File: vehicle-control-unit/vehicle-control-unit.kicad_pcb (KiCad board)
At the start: 2 copper layers, 175.3 x 50.8 mm, 53 parts, among them J1 Conn_02x04_Male_UnitPerRow, J10 Connector:Screw_Terminal_01x02, J2 Conn_01x04_Male, J3 Conn_02x03_Male, J4 Conn_02x03_Male, J5 Conn_02x03_Male, J6 Conn_02x03_Male, J7 Conn_01x03_Male, J8 Conn_01x03_Male, J9 Conn_02x06_Male_UnitPerRow, Q1 BC517, SW1 SW_SPST, U1 Teensy3.2, U2 NRF24L01+ breakout, U3 ULN2803A, U4 MIC29502WT

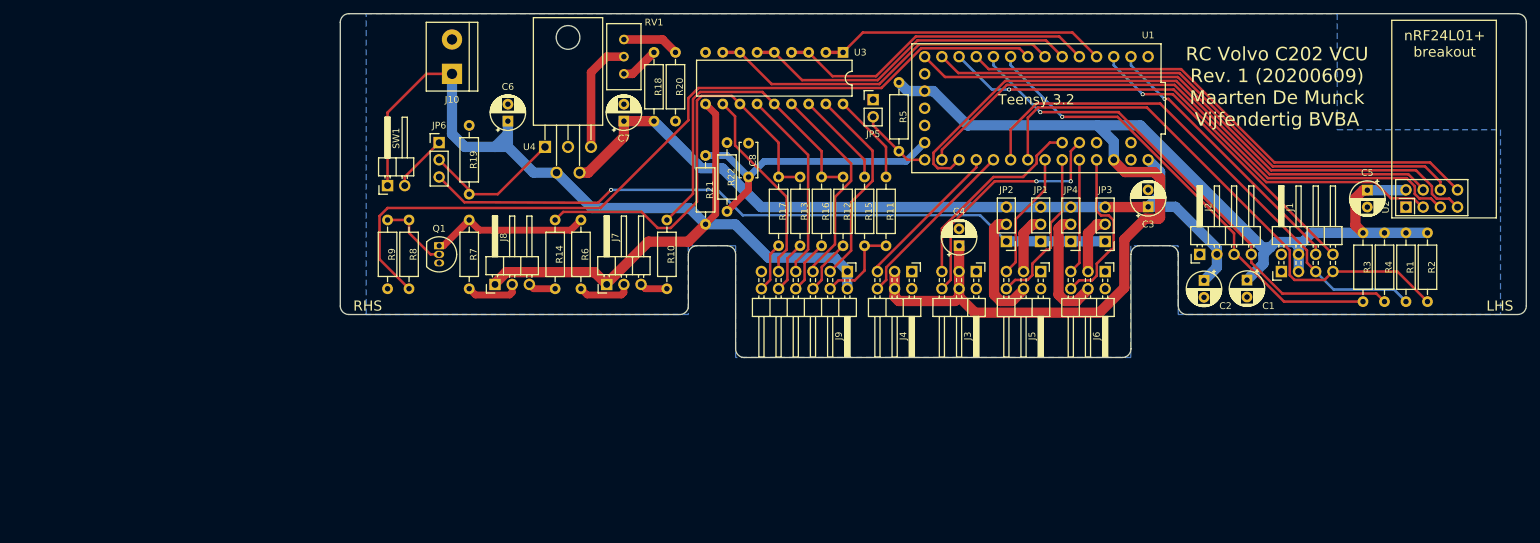
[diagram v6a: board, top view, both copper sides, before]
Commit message: Update VCU to KiCad 6.0
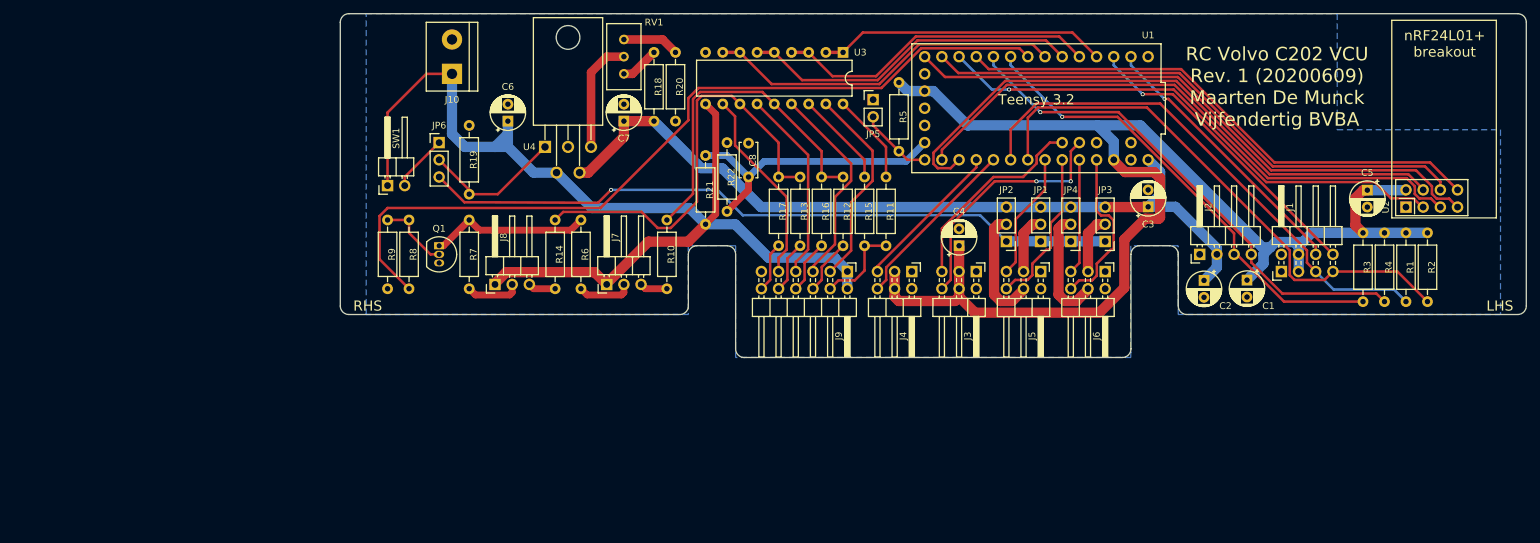
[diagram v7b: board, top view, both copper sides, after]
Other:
- outline, holes or cut-outs redrawn
- net class Default removed
